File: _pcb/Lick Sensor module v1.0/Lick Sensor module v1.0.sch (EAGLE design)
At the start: 5 parts

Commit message: update on VestibularVR & LickSensor
- returned to Eagle 9.6.2
- projects reviewed with Filipe
- LickSensor board with reviews already made
- VestibularVR  board starting implementing reviews
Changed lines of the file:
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@@
 <?xml version="1.0" encoding="utf-8"?>
 <!DOCTYPE eagle SYSTEM "eagle.dtd">
-<eagle version="8.3.1">
+<eagle version="9.6.2">
 <drawing>
 <settings>
@@
 <setting verticaltext="up"/>
 </settings>
-<grid distance="50" unitdist="mil" unit="mil" style="lines" multiple="1" display="yes" altdistance="0.01" altunitdist="inch" altunit="mil"/>
+<grid distance="0.1" unitdist="inch" unit="inch" style="lines" multiple="1" display="no" altdistance="0.01" altunitdist="inch" altunit="inch"/>
 <layers>
 <layer number="1" name="Top" color="4" fill="1" visible="no" active="no"/>
@@
 <attribute name="DIGKEYPN" x="138.43" y="68.58" size="1.778" layer="96" display="off"/>
 </instance>
-<instance part="LICK_PORT" gate="-1" x="148.59" y="73.66" rot="MR180"/>
-<instance part="LICK_PORT" gate="-2" x="148.59" y="76.2" rot="MR180"/>
-<instance part="LICK_PORT" gate="-3" x="148.59" y="78.74" rot="MR180"/>
+<instance part="LICK_PORT" gate="-1" x="148.59" y="73.66" smashed="yes" rot="MR180">
+<attribute name="NAME" x="151.13" y="74.422" size="1.524" layer="95" rot="MR180"/>
+<attribute name="VALUE" x="147.828" y="72.263" size="1.778" layer="96" rot="MR180"/>
+</instance>
+<instance part="LICK_PORT" gate="-2" x="148.59" y="76.2" smashed="yes" rot="MR180">
+<attribute name="NAME" x="151.13" y="76.962" size="1.524" layer="95" rot="MR180"/>
+</instance>
+<instance part="LICK_PORT" gate="-3" x="148.59" y="78.74" smashed="yes" rot="MR180">
+<attribute name="NAME" x="151.13" y="79.502" size="1.524" layer="95" rot="MR180"/>
+</instance>
 <instance part="+3V2" gate="G$1" x="91.44" y="68.58" smashed="yes" rot="MR0">
 <attribute name="VALUE" x="88.9" y="71.12" size="1.778" layer="96" rot="MR180"/>
 </instance>
-<instance part="FRAME1" gate="G$1" x="0" y="0"/>
-<instance part="C1" gate="G$1" x="124.46" y="88.9"/>
+<instance part="FRAME1" gate="G$1" x="0" y="0" smashed="yes">
+<attribute name="DRAWING_NAME" x="217.17" y="15.24" size="2.54" layer="94"/>
+<attribute name="LAST_DATE_TIME" x="217.17" y="10.16" size="2.286" layer="94"/>
+<attribute name="SHEET" x="230.505" y="5.08" size="2.54" layer="94"/>
+</instance>
+<instance part="C1" gate="G$1" x="124.46" y="88.9" smashed="yes">
+<attribute name="NAME" x="125.984" y="89.281" size="1.778" layer="95"/>
+<attribute name="VALUE" x="125.984" y="84.201" size="1.778" layer="96"/>
+</instance>
 <instance part="GND1" gate="1" x="124.46" y="80.01" smashed="yes">
 <attribute name="VALUE" x="121.92" y="77.47" size="1.778" layer="96"/>

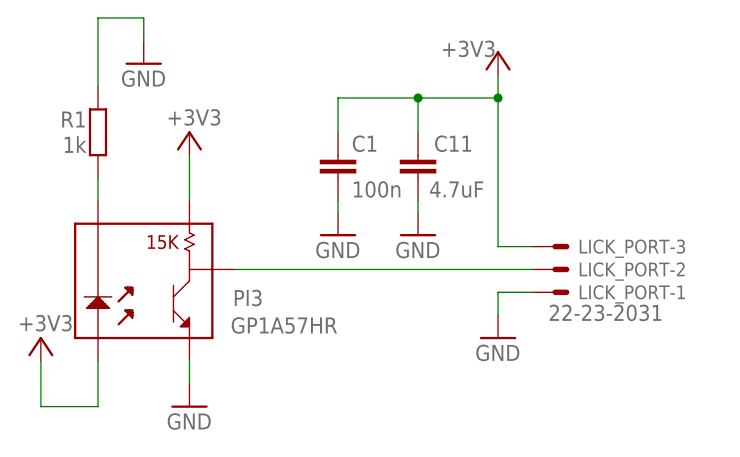
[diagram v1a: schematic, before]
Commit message: BOMs & start Harp Motor device H2-module v1.0
. almost final BOMs versions for VestibularVR H1-module v1.0 & Lick Sensor module v1.0
. start of new project Harp Motor device H2-module v1.0
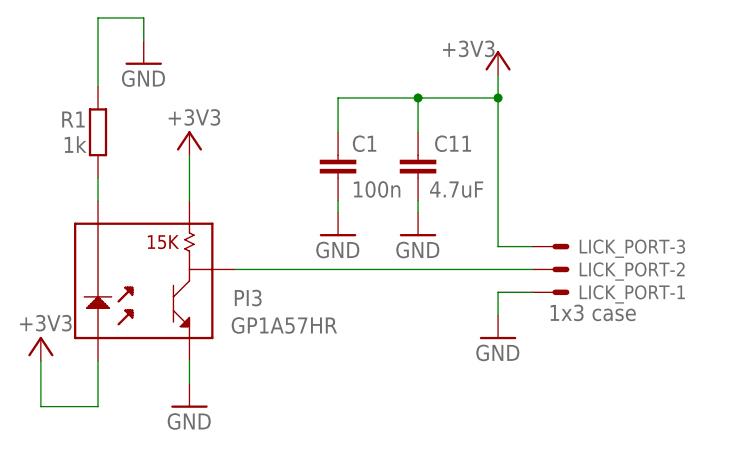
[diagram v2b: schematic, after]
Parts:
- C1: MPN (none) -> GRM155R71E104KE14D; OEPS (none) -> OEPS010004
- C11: NOTES - -> (none); OEPS (none) -> OEPS010018; TYPE SMD -> (none)
- LICK_PORT: value 22-23-2031 -> 1x3 case; MPN (none) -> 282834-3; OEPS (none) -> OEPS07 xxx2 Digikey A98334-ND
- PI3: DESCRIPTION (none) -> SENSOR OPTICAL 10MM PCB MOUNT; MPN (none) -> 282834-3 Digikey A98334-ND; OEPS (none) -> OEPSK01022
- R1: MPN (none) -> ERJ-2RKF1001X; OEPS (none) -> OEPS020006
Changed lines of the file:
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@@
 <parts>
 <part name="GND2" library="SparkFun" deviceset="GND" device=""/>
-<part name="PI3" library="SparkFun" deviceset="GP1A57HR" device=""/>
-<part name="R1" library="rcl" library_urn="urn:adsk.eagle:library:334" deviceset="R-EU_" device="R0603" package3d_urn="urn:adsk.eagle:package:23555/2" value="1k"/>
+<part name="PI3" library="SparkFun" deviceset="GP1A57HR" device="">
+<attribute name="DESCRIPTION" value="SENSOR OPTICAL 10MM PCB MOUNT"/>
+<attribute name="MPN" value="282834-3
+Digikey A98334-ND"/>
+<attribute name="OEPS" value="OEPSK01022"/>
+</part>
+<part name="R1" library="rcl" library_urn="urn:adsk.eagle:library:334" deviceset="R-EU_" device="R0603" package3d_urn="urn:adsk.eagle:package:23555/2" value="1k">
+<attribute name="MPN" value="ERJ-2RKF1001X"/>
+<attribute name="OEPS" value="OEPS020006"/>
+</part>
 <part name="GND34" library="SparkFun" deviceset="GND" device=""/>
 <part name="+3V8" library="supply1" deviceset="+3V3" device=""/>
@@
 <attribute name="DIGKEYPN" value=""/>
 </part>
-<part name="LICK_PORT" library="con-molex" library_urn="urn:adsk.eagle:library:165" deviceset="22-23-2031" device=""/>
+<part name="LICK_PORT" library="con-molex" library_urn="urn:adsk.eagle:library:165" deviceset="22-23-2031" device="" value="1x3 case">
+<attribute name="MPN" value="282834-3"/>
+<attribute name="OEPS" value="OEPS07 xxx2   Digikey A98334-ND"/>
+</part>
 <part name="+3V2" library="supply1" deviceset="+3V3" device=""/>
 <part name="FRAME1" library="frames" library_urn="urn:adsk.eagle:library:229" deviceset="A4L-LOC" device=""/>
-<part name="C1" library="rcl" library_urn="urn:adsk.eagle:library:334" deviceset="C-EU" device="C0402K" package3d_urn="urn:adsk.eagle:package:23679/2" value="100n"/>
+<part name="C1" library="rcl" library_urn="urn:adsk.eagle:library:334" deviceset="C-EU" device="C0402K" package3d_urn="urn:adsk.eagle:package:23679/2" value="100n">
+<attribute name="MPN" value="GRM155R71E104KE14D"/>
+<attribute name="OEPS" value="OEPS010004"/>
+</part>
 <part name="GND1" library="SparkFun" deviceset="GND" device=""/>
 <part name="+3V1" library="supply1" deviceset="+3V3" device=""/>
 <part name="C11" library="rcl" deviceset="C-EU" device="C0603" value="4.7uF">
 <attribute name="MPN" value="C1608X6S1C475K080AC"/>
-<attribute name="NOTES" value="-"/>
-<attribute name="TYPE" value="SMD"/>
+<attribute name="OEPS" value="OEPS010018"/>
 </part>
 <part name="GND3" library="SparkFun" deviceset="GND" device=""/>
@@
 <attribute name="NAME" x="112.776" y="72.136" size="1.778" layer="95"/>
 <attribute name="VALUE" x="112.522" y="69.088" size="1.778" layer="96"/>
+<attribute name="OEPS" x="102.87" y="71.12" size="1.778" layer="96" display="off"/>
+<attribute name="DESCRIPTION" x="102.87" y="71.12" size="1.778" layer="96" display="off"/>
+<attribute name="MPN" x="102.87" y="71.12" size="1.778" layer="96" display="off"/>
 </instance>
 <instance part="R1" gate="G$1" x="97.79" y="91.44" smashed="yes" rot="R90">
 <attribute name="NAME" x="96.52" y="93.7514" size="1.778" layer="95" rot="R180"/>
 <attribute name="VALUE" x="96.52" y="90.932" size="1.778" layer="96" rot="R180"/>
+<attribute name="OEPS" x="97.79" y="91.44" size="1.778" layer="96" rot="R90" display="off"/>
+<attribute name="MPN" x="97.79" y="91.44" size="1.778" layer="96" rot="R90" display="off"/>
 </instance>
 <instance part="GND34" gate="1" x="102.87" y="99.06" smashed="yes">
@@
 <instance part="LICK_PORT" gate="-2" x="148.59" y="76.2" smashed="yes" rot="MR180">
 <attribute name="NAME" x="151.13" y="76.962" size="1.524" layer="95" rot="MR180"/>
+<attribute name="OEPS" x="148.59" y="76.2" size="1.778" layer="96" rot="MR180" display="off"/>
 </instance>
 <instance part="LICK_PORT" gate="-3" x="148.59" y="78.74" smashed="yes" rot="MR180">
@@
 <attribute name="NAME" x="125.984" y="89.281" size="1.778" layer="95"/>
 <attribute name="VALUE" x="125.984" y="84.201" size="1.778" layer="96"/>
+<attribute name="OEPS" x="124.46" y="88.9" size="1.778" layer="96" display="off"/>
+<attribute name="MPN" x="124.46" y="88.9" size="1.778" layer="96" display="off"/>
 </instance>
 <instance part="GND1" gate="1" x="124.46" y="80.01" smashed="yes">
@@
 <attribute name="NAME" x="139.446" y="89.281" size="1.778" layer="95" rot="MR0"/>
 <attribute name="VALUE" x="140.716" y="84.201" size="1.778" layer="96" rot="MR0"/>
+<attribute name="OEPS" x="133.35" y="88.9" size="1.778" layer="96" rot="MR0" display="off"/>
 <attribute name="MPN" x="133.35" y="88.9" size="1.778" layer="96" rot="MR0" display="off"/>
-<attribute name="TYPE" x="133.35" y="88.9" size="1.778" layer="96" rot="MR0" display="off"/>
-<attribute name="NOTES" x="133.35" y="88.9" size="1.778" layer="96" rot="MR0" display="off"/>
 </instance>
 <instance part="GND3" gate="1" x="133.35" y="80.01" smashed="yes">

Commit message: VestibularVR H1 module & Lick Sensor module v1.0 FINAL BOMs
final BOM versions
. VestibularVR H1 module
. Lick Sensor module v1.0
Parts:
- LICK_PORT: OEPS OEPS07 xxx2 Digikey A98334-ND -> OEPS070035
- PI3: MPN 282834-3 Digikey A98334-ND -> GP1A57HRJ00F
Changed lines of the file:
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@@
 <part name="PI3" library="SparkFun" deviceset="GP1A57HR" device="">
 <attribute name="DESCRIPTION" value="SENSOR OPTICAL 10MM PCB MOUNT"/>
-<attribute name="MPN" value="282834-3
-Digikey A98334-ND"/>
+<attribute name="MPN" value="GP1A57HRJ00F"/>
 <attribute name="OEPS" value="OEPSK01022"/>
 </part>
@@
 <part name="LICK_PORT" library="con-molex" library_urn="urn:adsk.eagle:library:165" deviceset="22-23-2031" device="" value="1x3 case">
 <attribute name="MPN" value="282834-3"/>
-<attribute name="OEPS" value="OEPS07 xxx2   Digikey A98334-ND"/>
+<attribute name="OEPS" value="OEPS070035"/>
 </part>
 <part name="+3V2" library="supply1" deviceset="+3V3" device=""/>
